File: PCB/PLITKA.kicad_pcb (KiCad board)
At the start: 2 copper layers, 120.5 x 85.5 mm, 47 parts, among them SW1 MX_SW_HS, SW10 MX_SW_HS, SW11 MX_SW_HS, SW12 MX_SW_HS, SW13 MX_SW_HS, SW14 MX_SW_HS, SW15 MX_SW_HS, SW16 MX_SW_HS, SW17 MX_SW_HS, SW2 MX_SW_HS, SW3 MX_SW_HS, SW4 MX_SW_HS, SW5 MX_SW_HS, SW6 MX_SW_HS, SW7 MX_SW_HS, SW8 MX_SW_HS, SW9 MX_SW_HS, U1 nice!nano

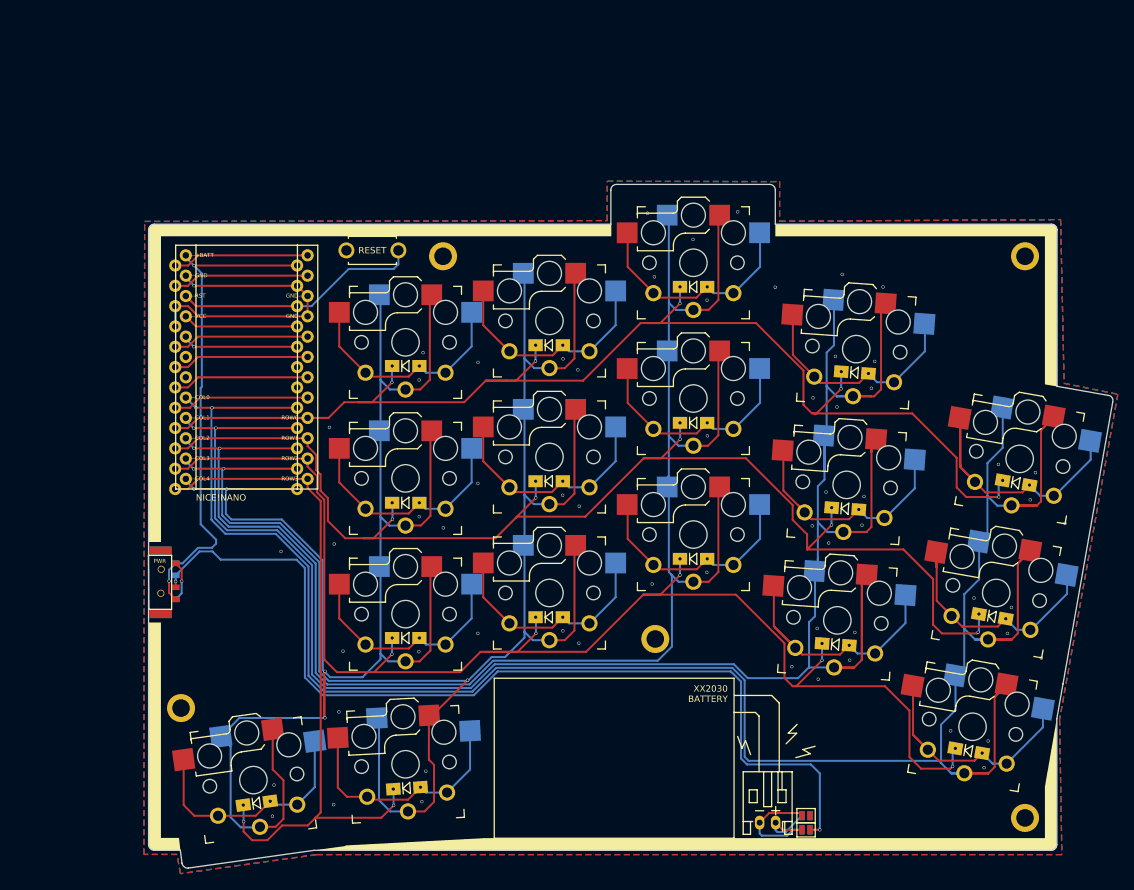
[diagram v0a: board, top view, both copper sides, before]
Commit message: Corrections to the symbol pads oredering and other definitions
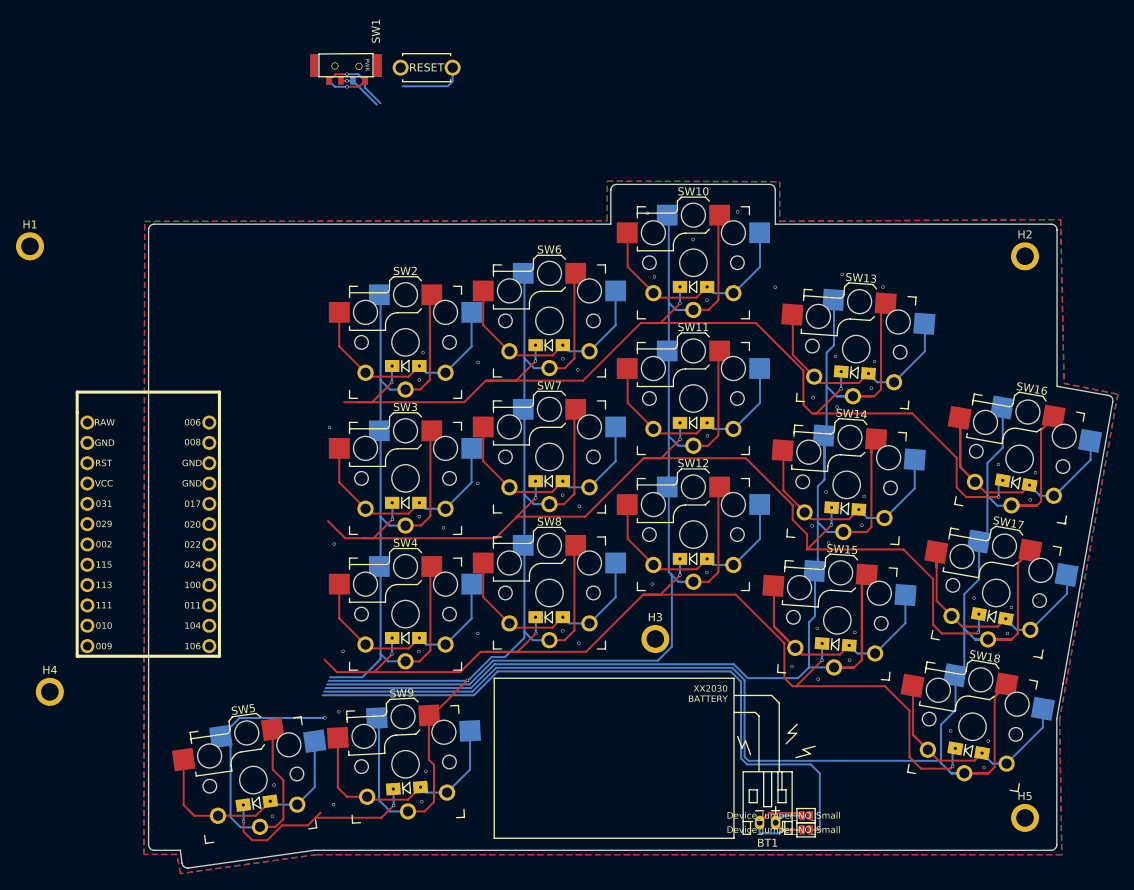
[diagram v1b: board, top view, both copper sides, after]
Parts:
- U1: footprint PLITKA:ProMicro_v2 -> PLITKA:nice_nano
- moved SW1 68.2 mm to (113.4, 32.4), turned to -90 degrees
- moved H1 51.6 mm to (70.0, 56.3)
- moved SW19 23.8 mm to (119.6, 34.0)
- moved U1 21.1 mm to (86.8, 90.3)
- moved H4 16.5 mm to (72.5, 112.0)
- renumbered D8 to D10, D13 to D11, D4 to D12, D9 to D13, D5 to D15, D10 to D16, D15 to D17, D6 to D2, D11 to D3, D16 to D4, D2 to D5, D7 to D6, D12 to D7, D17 to D8, D3 to D9, MH1 to H1, MH2 to H2, MH3 to H3, MH4 to H4, MH5 to H5, PSW1 to SW1, SW3 to SW10, SW8 to SW11, SW13 to SW12, SW4 to SW13, SW9 to SW14, SW14 to SW15, SW5 to SW16, SW10 to SW17, SW15 to SW18, RSW1 to SW19, SW1 to SW2, SW6 to SW3, SW11 to SW4, SW16 to SW5, SW2 to SW6, SW12 to SW8, SW17 to SW9
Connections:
- D1 pad 1: row0 -> row_A
- D10 pad 1: row1 -> row_B
- D11 pad 1: row2 -> row_C
- D12 pad 1: row0 -> row_A
- D13 pad 1: row1 -> row_B
- D14 pad 1: row2 -> row_C
- D15 pad 1: row0 -> row_A
- D16 pad 1: row1 -> row_B
- D17 pad 1: row2 -> row_C
- D2 pad 1: row1 -> row_B
- D3 pad 1: row2 -> row_C
- D4 pad 1: row3 -> row_D
- D5 pad 1: row0 -> row_A
- D6 pad 1: row1 -> row_B
- D7 pad 1: row2 -> row_C
- D8 pad 1: row3 -> row_D
- D9 pad 1: row0 -> row_A
- SW10 pad 1: col2 -> col_C
- SW11 pad 1: col2 -> col_C
- SW12 pad 1: col2 -> col_C
- SW13 pad 1: col1 -> col_D
- SW14 pad 1: col1 -> col_D
- SW15 pad 1: col1 -> col_D
- SW16 pad 1: col0 -> col_E
- SW17 pad 1: col0 -> col_E
- SW18 pad 1: col0 -> col_E
- SW2 pad 1: col4 -> col_A
- SW3 pad 1: col4 -> col_A
- SW4 pad 1: col4 -> col_A
- SW5 pad 1: col4 -> col_A
- SW6 pad 1: col3 -> col_B
- SW7 pad 1: col3 -> col_B
- SW8 pad 1: col3 -> col_B
- SW9 pad 1: col3 -> col_B
- U1 pad 10: row1 -> row_A
- U1 pad 11: row2 -> row_B
- U1 pad 12: row3 -> row_C
- U1 pad 13: col4 -> VBAT
- U1 pad 14: col3 -> GND
- U1 pad 15: col2 -> RESET
- U1 pad 16: col1 -> VCC
- U1 pad 17: col0 -> unconnected-(U1-D21/P0.31-Pad17)
- U1 pad 21: VCC -> unconnected-(U1-D15/P1.13-Pad21)
- U1 pad 22: RESET -> unconnected-(U1-D14/P1.11-Pad22)
- U1 pad 23: GND -> unconnected-(U1-D16/P0.10-Pad23)
- U1 pad 24: +BATT -> row_D
- U1 pad 3: GND -> unconnected-(U1-GND-Pad3)
- U1 pad 4: GND -> unconnected-(U1-GND-Pad4)
- U1 pad 5: unconnected-(U1-2/D1/SDA-Pad5) -> col_A
- U1 pad 6: unconnected-(U1-3/D0/SCL-Pad6)_1 -> col_B
- U1 pad 7: unconnected-(U1-4/D4-Pad7) -> col_C
- U1 pad 8: unconnected-(U1-5/C6-Pad8)_1 -> col_D
- U1 pad 9: row0 -> col_E
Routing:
- net col0: track 271.0 -> 0.00 mm, vias 2 -> 0
- net col1: track 256.8 -> 0.00 mm, vias 2 -> 0
- net col_E: track 0.00 -> 211.6 mm
- net col3: track 209.9 -> 0.00 mm, vias 3 -> 0
- net col4: track 206.5 -> 0.00 mm, vias 4 -> 0
- net col2: track 204.6 -> 0.00 mm, vias 2 -> 0
- net col_D: track 0.00 -> 200.5 mm
- net row2: track 171.9 -> 0.00 mm, vias 5 -> 0
- net col_B: track 0.00 -> 159.8 mm, vias 0 -> 1
- net row1: track 158.0 -> 0.00 mm, vias 5 -> 0
- net row0: track 154.1 -> 0.00 mm, vias 5 -> 0
- net col_C: track 0.00 -> 151.4 mm
- net col_A: track 0.00 -> 148.8 mm, vias 0 -> 1
- net row_A: track 0.00 -> 131.6 mm, vias 0 -> 5
- net row_B: track 0.00 -> 129.6 mm, vias 0 -> 5
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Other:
- board text removed: "--+BATT"
- board text removed: "--COL0"
- board text removed: "--COL1"
- board text removed: "--COL2"
- board text removed: "--COL3"
- board text removed: "--COL4"
- board text removed: "--GND"
- board text removed: "--RST"
- board text removed: "--VCC"
- board text removed: "GND--"
- board text removed: "NICE!NANO"
- board text removed: "ROW0--"
- board text removed: "ROW1--"
- board text removed: "ROW2--"
- board text removed: "ROW3--"

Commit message: Corrected the references to the footprints
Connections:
- U1 pad 13: VBAT -> +BATT
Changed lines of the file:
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@@
 			)
 		)
-		(attr through_hole dnp)
+		(attr through_hole)
 		(duplicate_pad_numbers_are_jumpers no)
 		(fp_line
@@
 			)
 		)
-		(attr through_hole dnp)
+		(attr through_hole)
 		(duplicate_pad_numbers_are_jumpers no)
 		(fp_line
@@
 			)
 		)
-		(attr through_hole dnp)
+		(attr through_hole)
 		(duplicate_pad_numbers_are_jumpers no)
 		(fp_line
@@
 			)
 		)
-		(attr through_hole dnp)
+		(attr through_hole)
 		(duplicate_pad_numbers_are_jumpers no)
 		(fp_line
@@
 			)
 		)
-		(attr through_hole dnp)
+		(attr through_hole)
 		(duplicate_pad_numbers_are_jumpers no)
 		(fp_line
@@
 			)
 		)
-		(attr through_hole dnp)
+		(attr through_hole)
 		(duplicate_pad_numbers_are_jumpers no)
 		(fp_line
@@
 			)
 		)
-		(attr through_hole dnp)
+		(attr through_hole)
 		(duplicate_pad_numbers_are_jumpers no)
 		(fp_line
@@
 			)
 		)
-		(attr through_hole dnp)
+		(attr through_hole)
 		(duplicate_pad_numbers_are_jumpers no)
 		(fp_line
@@
 			)
 		)
-		(attr through_hole dnp)
+		(attr through_hole)
 		(duplicate_pad_numbers_are_jumpers no)
 		(fp_line
@@
 			)
 		)
-		(attr through_hole dnp)
+		(attr through_hole)
 		(duplicate_pad_numbers_are_jumpers no)
 		(fp_line
@@
 			)
 		)
-		(attr through_hole dnp)
+		(attr through_hole)
 		(duplicate_pad_numbers_are_jumpers no)
 		(fp_line
@@
 			)
 		)
-		(attr through_hole dnp)
+		(attr through_hole)
 		(duplicate_pad_numbers_are_jumpers no)
 		(fp_line
@@
 			)
 		)
-		(attr through_hole dnp)
+		(attr through_hole)
 		(duplicate_pad_numbers_are_jumpers no)
 		(fp_line
@@
 			)
 		)
-		(attr through_hole dnp)
+		(attr through_hole)
 		(duplicate_pad_numbers_are_jumpers no)
 		(fp_line
@@
 			)
 		)
-		(attr through_hole dnp)
+		(attr through_hole)
 		(duplicate_pad_numbers_are_jumpers no)
 		(fp_line
@@
 			)
 		)
-		(attr through_hole dnp)
+		(attr through_hole)
 		(duplicate_pad_numbers_are_jumpers no)
 		(fp_line
@@
 			(layers "*.Cu" "*.SilkS" "*.Mask")
 			(remove_unused_layers no)
-			(net "VBAT")
+			(net "+BATT")
 			(pinfunction "VBAT_13")
 			(pintype "power_out")
@@
 			)
 		)
-		(attr through_hole dnp)
+		(attr through_hole)
 		(duplicate_pad_numbers_are_jumpers no)
 		(fp_line
